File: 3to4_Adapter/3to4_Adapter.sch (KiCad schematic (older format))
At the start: 11 parts, among them J1 v3 Header, J2 v4 Output, J3 CLK_GND, U1 AMS1117-3.3

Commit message: Created BOM
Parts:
- C1, C2: Digi-Key_PN (none) -> 1189-4000-ND; MPN (none) -> 35ZLG10MEFC5X7
- J3: Digi-Key_PN (none) -> 732-5315-ND; MPN (none) -> 61300211121
- R1: Digi-Key_PN (none) -> CF14JT10K0TR-ND; MPN (none) -> CF14JT10K0
- U1: Digi-Key_PN (none) -> AP2111H-3.3TRG1DICT-ND; MPN (none) -> AP2111H-3.3TRG1
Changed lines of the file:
@@
 F 2 "Package_TO_SOT_SMD:SOT-223-3_TabPin2" H 6750 3500 50  0001 C CNN
 F 3 "http://www.advanced-monolithic.com/pdf/ds1117.pdf" H 6850 3050 50  0001 C CNN
+F 4 "AP2111H-3.3TRG1DICT-ND" H 6750 3300 50  0001 C CNN "Digi-Key_PN"
+F 5 "AP2111H-3.3TRG1" H 6750 3300 50  0001 C CNN "MPN"
 	1    6750 3300
 	1    0    0    -1
@@
 F 2 "Capacitor_THT:CP_Radial_D5.0mm_P2.00mm" H 7688 3250 50  0001 C CNN
 F 3 "~" H 7650 3400 50  0001 C CNN
+F 4 "1189-4000-ND" H 7650 3400 50  0001 C CNN "Digi-Key_PN"
+F 5 "35ZLG10MEFC5X7" H 7650 3400 50  0001 C CNN "MPN"
 	1    7650 3400
 	1    0    0    -1
@@
 F 2 "Capacitor_THT:CP_Radial_D5.0mm_P2.00mm" H 5938 3150 50  0001 C CNN
 F 3 "~" H 5900 3300 50  0001 C CNN
+F 4 "1189-4000-ND" H 5900 3300 50  0001 C CNN "Digi-Key_PN"
+F 5 "35ZLG10MEFC5X7" H 5900 3300 50  0001 C CNN "MPN"
 	1    5900 3300
 	1    0    0    -1
@@
 F 2 "Resistor_THT:R_Axial_DIN0207_L6.3mm_D2.5mm_P7.62mm_Horizontal" V 2230 4200 50  0001 C CNN
 F 3 "~" H 2300 4200 50  0001 C CNN
+F 4 "CF14JT10K0TR-ND" H 2300 4200 50  0001 C CNN "Digi-Key_PN"
+F 5 "CF14JT10K0" H 2300 4200 50  0001 C CNN "MPN"
 	1    2300 4200
 	0    1    1    0
@@
 F 2 "Connector_PinHeader_2.54mm:PinHeader_1x02_P2.54mm_Vertical" H 2050 3550 50  0001 C CNN
 F 3 "~" H 2050 3550 50  0001 C CNN
+F 4 "732-5315-ND" H 2050 3550 50  0001 C CNN "Digi-Key_PN"
+F 5 "61300211121" H 2050 3550 50  0001 C CNN "MPN"
 	1    2050 3550
 	1    0    0    -1

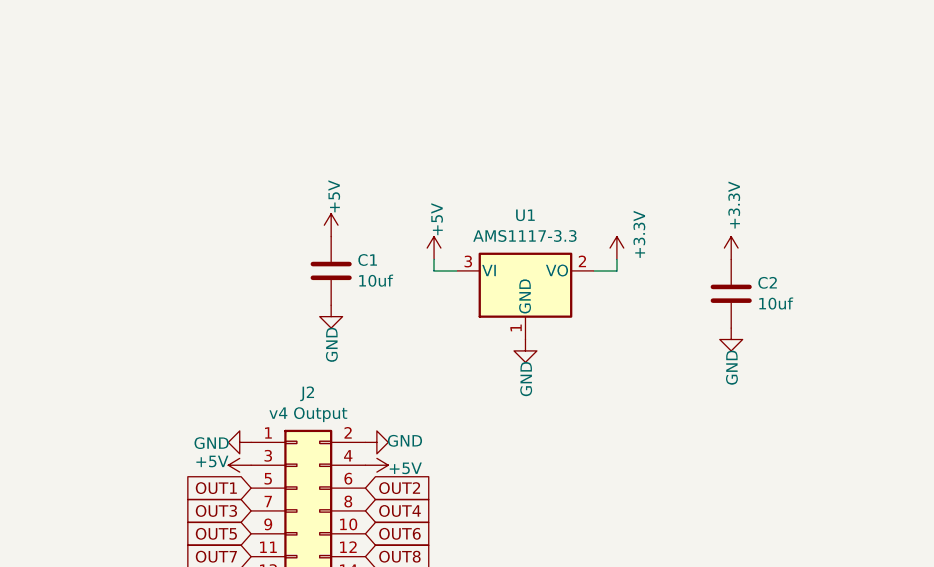
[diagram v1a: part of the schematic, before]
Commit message: added 3.3v jumper
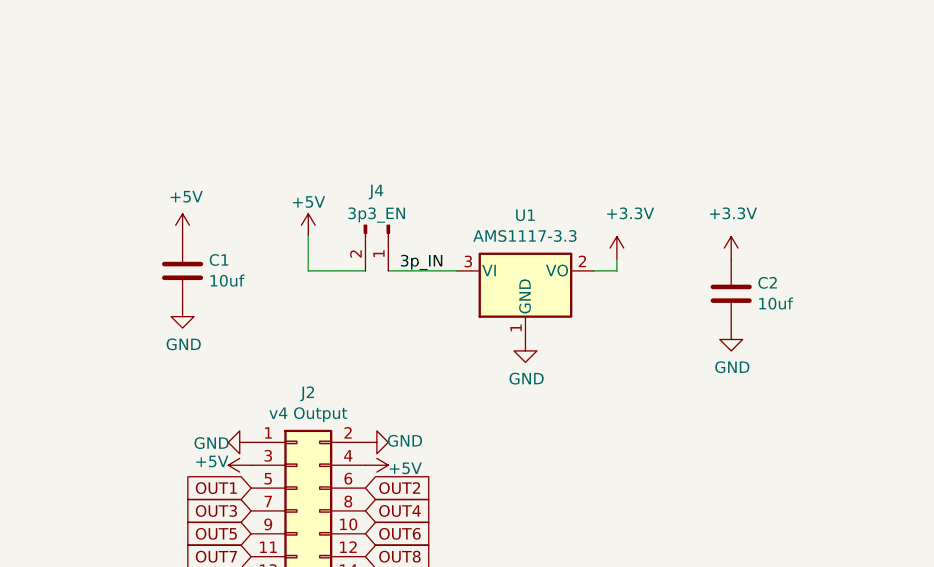
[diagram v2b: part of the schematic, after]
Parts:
- added J4: 3p3_EN, Connector_PinHeader_2.54mm:PinHeader_1x02_P2.54mm_Vertical, symbol Connector:Conn_01x02_Male
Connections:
- net +5V: now also J4.2 (Pin_2); no longer U1.3 (VI)
- new net 3p_IN: J4.1 (Pin_1), U1.3 (VI)
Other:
- moved on the sheet: C1
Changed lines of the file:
@@
 Sheet 1 1
 Title "v3 to v4"
-Date "2021-08-28"
-Rev "v1"
+Date "2021-09-03"
+Rev "v2"
 Comp "Scott Hanson"
 Comment1 ""
@@
 L Device:C C1
 U 1 1 612C6071
-P 5900 3300
-F 0 "C1" H 6015 3346 50  0000 L CNN
-F 1 "10uf" H 6015 3255 50  0000 L CNN
-F 2 "Capacitor_THT:CP_Radial_D5.0mm_P2.00mm" H 5938 3150 50  0001 C CNN
-F 3 "~" H 5900 3300 50  0001 C CNN
-F 4 "1189-4000-ND" H 5900 3300 50  0001 C CNN "Digi-Key_PN"
-F 5 "35ZLG10MEFC5X7" H 5900 3300 50  0001 C CNN "MPN"
-	1    5900 3300
+P 5250 3300
+F 0 "C1" H 5365 3346 50  0000 L CNN
+F 1 "10uf" H 5365 3255 50  0000 L CNN
+F 2 "Capacitor_THT:CP_Radial_D5.0mm_P2.00mm" H 5288 3150 50  0001 C CNN
+F 3 "~" H 5250 3300 50  0001 C CNN
+F 4 "1189-4000-ND" H 5250 3300 50  0001 C CNN "Digi-Key_PN"
+F 5 "35ZLG10MEFC5X7" H 5250 3300 50  0001 C CNN "MPN"
+	1    5250 3300
 	1    0    0    -1
 $EndComp
@@
 P 7150 3250
 F 0 "#PWR010" H 7150 3100 50  0001 C CNN
-F 1 "+3.3V" V 7250 3250 50  0000 L CNN
+F 1 "+3.3V" H 7100 3450 50  0000 L CNN
 F 2 "" H 7150 3250 50  0001 C CNN
 F 3 "" H 7150 3250 50  0001 C CNN
@@
 P 7650 3250
 F 0 "#PWR011" H 7650 3100 50  0001 C CNN
-F 1 "+3.3V" V 7665 3378 50  0000 L CNN
+F 1 "+3.3V" H 7550 3450 50  0000 L CNN
 F 2 "" H 7650 3250 50  0001 C CNN
 F 3 "" H 7650 3250 50  0001 C CNN
@@
 L power:+5V #PWR08
 U 1 1 612CD44C
-P 6350 3250
-F 0 "#PWR08" H 6350 3100 50  0001 C CNN
-F 1 "+5V" V 6365 3423 50  0000 C CNN
-F 2 "" H 6350 3250 50  0001 C CNN
-F 3 "" H 6350 3250 50  0001 C CNN
-	1    6350 3250
+P 5800 3150
+F 0 "#PWR08" H 5800 3000 50  0001 C CNN
+F 1 "+5V" H 5800 3300 50  0000 C CNN
+F 2 "" H 5800 3150 50  0001 C CNN
+F 3 "" H 5800 3150 50  0001 C CNN
+	1    5800 3150
 	1    0    0    -1
 $EndComp
@@
 L power:+5V #PWR04
 U 1 1 612CE662
-P 5900 3150
-F 0 "#PWR04" H 5900 3000 50  0001 C CNN
-F 1 "+5V" V 5915 3323 50  0000 C CNN
-F 2 "" H 5900 3150 50  0001 C CNN
-F 3 "" H 5900 3150 50  0001 C CNN
-	1    5900 3150
+P 5250 3150
+F 0 "#PWR04" H 5250 3000 50  0001 C CNN
+F 1 "+5V" H 5265 3323 50  0000 C CNN
+F 2 "" H 5250 3150 50  0001 C CNN
+F 3 "" H 5250 3150 50  0001 C CNN
+	1    5250 3150
 	1    0    0    -1
 $EndComp
@@
 P 6750 3600
 F 0 "#PWR09" H 6750 3350 50  0001 C CNN
-F 1 "GND" V 6755 3427 50  0000 C CNN
+F 1 "GND" H 6755 3427 50  0000 C CNN
 F 2 "" H 6750 3600 50  0001 C CNN
 F 3 "" H 6750 3600 50  0001 C CNN
@@
 P 7650 3550
 F 0 "#PWR012" H 7650 3300 50  0001 C CNN
-F 1 "GND" V 7655 3377 50  0000 C CNN
+F 1 "GND" H 7655 3377 50  0000 C CNN
 F 2 "" H 7650 3550 50  0001 C CNN
 F 3 "" H 7650 3550 50  0001 C CNN
@@
 L power:GND #PWR05
 U 1 1 612D1C16
-P 5900 3450
-F 0 "#PWR05" H 5900 3200 50  0001 C CNN
-F 1 "GND" V 5905 3277 50  0000 C CNN
-F 2 "" H 5900 3450 50  0001 C CNN
-F 3 "" H 5900 3450 50  0001 C CNN
-	1    5900 3450
+P 5250 3450
+F 0 "#PWR05" H 5250 3200 50  0001 C CNN
+F 1 "GND" H 5255 3277 50  0000 C CNN
+F 2 "" H 5250 3450 50  0001 C CNN
+F 3 "" H 5250 3450 50  0001 C CNN
+	1    5250 3450
 	1    0    0    -1
 $EndComp
@@
 Wire Wire Line
 	7150 3300 7150 3250
-Wire Wire Line
-	6350 3250 6350 3300
-Wire Wire Line
-	6350 3300 6450 3300
 Text GLabel 5550 5050 0    50   Input ~ 0
 CLK
@@
 Text GLabel 3800 4650 2    50   Input ~ 0
 CLK_V3
+$Comp
+L Connector:Conn_01x02_Male J4
+U 1 1 619E54EB
+P 6150 3100
+F 0 "J4" V 6000 3050 50  0000 C CNN
+F 1 "3p3_EN" V 6100 3050 50  0000 C CNN
+F 2 "Connector_PinHeader_2.54mm:PinHeader_1x02_P2.54mm_Vertical" H 6150 3100 50  0001 C CNN
+F 3 "~" H 6150 3100 50  0001 C CNN
+F 4 "732-5315-ND" H 6150 3100 50  0001 C CNN "Digi-Key_PN"
+F 5 "61300211121" H 6150 3100 50  0001 C CNN "MPN"
+	1    6150 3100
+	0    1    1    0
+$EndComp
+Wire Wire Line
+	5800 3150 5800 3300
+Wire Wire Line
+	5800 3300 6050 3300
+Wire Wire Line
+	6150 3300 6450 3300
+Text Label 6200 3300 0    50   ~ 0
+3p_IN
 $EndSCHEMATC

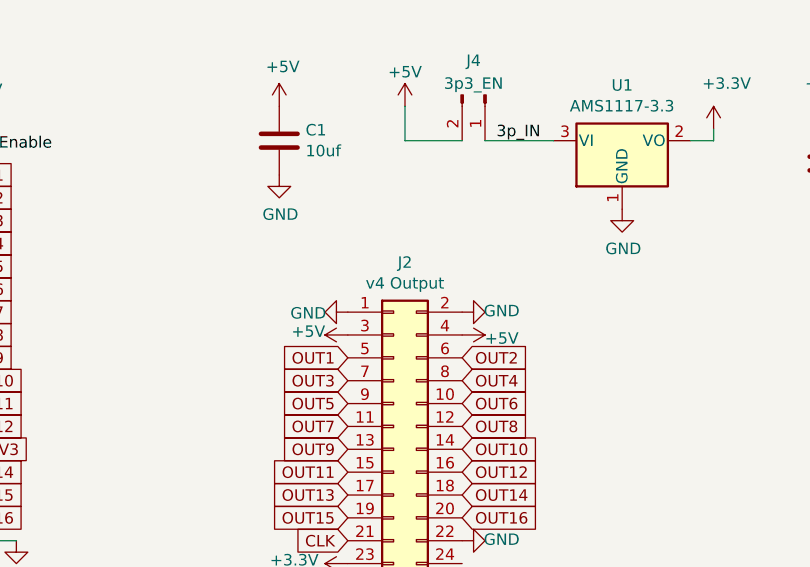
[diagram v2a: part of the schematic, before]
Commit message: swapped header
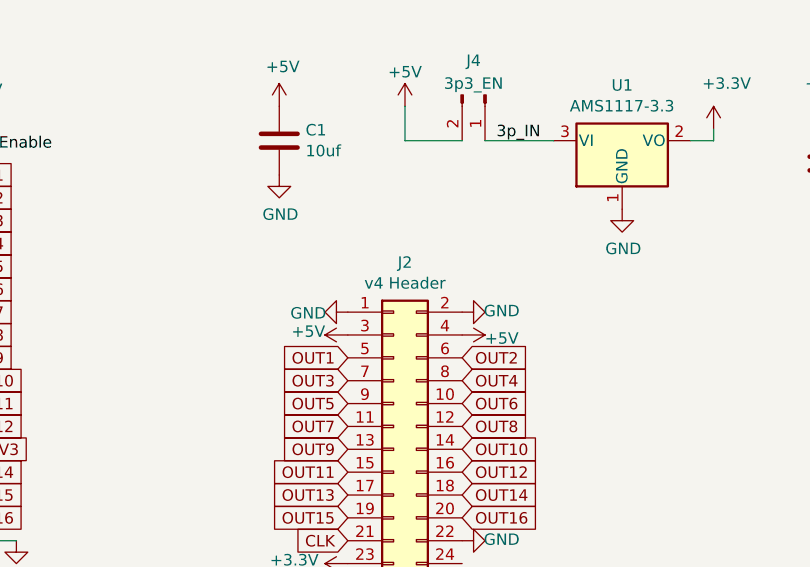
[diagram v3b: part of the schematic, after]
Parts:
- J2: value v4 Output -> v4 Header
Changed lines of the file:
@@
 P 5750 4550
 F 0 "J2" H 5800 5267 50  0000 C CNN
-F 1 "v4 Output" H 5800 5176 50  0000 C CNN
+F 1 "v4 Header" H 5800 5176 50  0000 C CNN
 F 2 "302-S241:OST_302-S241" H 5750 4550 50  0001 C CNN
 F 3 "~" H 5750 4550 50  0001 C CNN
